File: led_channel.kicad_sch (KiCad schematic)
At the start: 2 parts, among them Q1 SSM3K329R

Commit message: Rev 2
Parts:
- added R13: 1k, Resistor_SMD:R_0603_1608Metric, symbol Device:R
- R1: value 10k -> 100k
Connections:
- net SIGNAL: now also R13.1; no longer Q1.1 (G), R1.1
- new net: Q1.1 (G), R1.1, R13.2

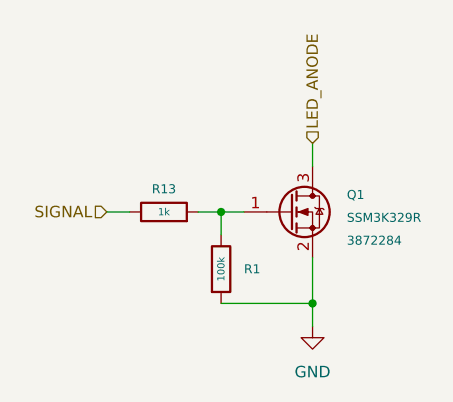
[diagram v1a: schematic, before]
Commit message: Fix comp refs, replace LDO with easier one easier to get
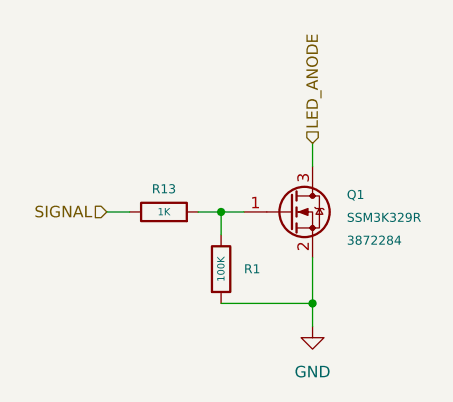
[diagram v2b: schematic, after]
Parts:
- Q1: LCSC (none) -> C150127; MFR (none) -> SSM3K329R
- R1: value 100k -> 100K
- R13: value 1k -> 1K
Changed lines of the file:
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@@
       (effects (font (size 1 1)))
     )
-    (property "Value" "1k" (at 109.22 86.36 90)
+    (property "Value" "1K" (at 109.22 86.36 90)
       (effects (font (size 0.8 0.8)))
     )
@@
     )
     (property "Datasheet" "~" (at 109.22 86.36 0)
+      (effects (font (size 1.27 1.27)) hide)
+    )
+    (property "MFR" "" (at 109.22 86.36 0)
       (effects (font (size 1.27 1.27)) hide)
     )
@@
       (effects (font (size 1 1)) (justify left))
     )
+    (property "MFR" "SSM3K329R" (at 123.19 86.36 0)
+      (effects (font (size 1.27 1.27)) hide)
+    )
+    (property "LCSC" "C150127" (at 123.19 86.36 0)
+      (effects (font (size 1.27 1.27)) hide)
+    )
     (pin "1")
     (pin "2")
@@
       (effects (font (size 1 1)) (justify left))
     )
-    (property "Value" "100k" (at 115.57 92.71 90)
+    (property "Value" "100K" (at 115.57 92.71 90)
       (effects (font (size 0.8 0.8)))
     )
@@
       (effects (font (size 1.27 1.27)) hide)
     )
+    (property "MFR" "" (at 115.57 92.71 0)
+      (effects (font (size 1.27 1.27)) hide)
+    )
